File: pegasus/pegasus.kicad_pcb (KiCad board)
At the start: 2 copper layers, 50 x 120 mm, 10 parts, among them IC1 RFD900, IC2 Adafruit_MPL3115A2, IC3 Adafruit-BNO055-PCB, IC4 L70B-M39, IC5 L7805ACV, J1 Conn_01x02_Female, J2 Conn_01x02_Female, U1 Teensy4.1, U2 CON-SMA-EDGE-S, U3 CON-SMA-EDGE-S

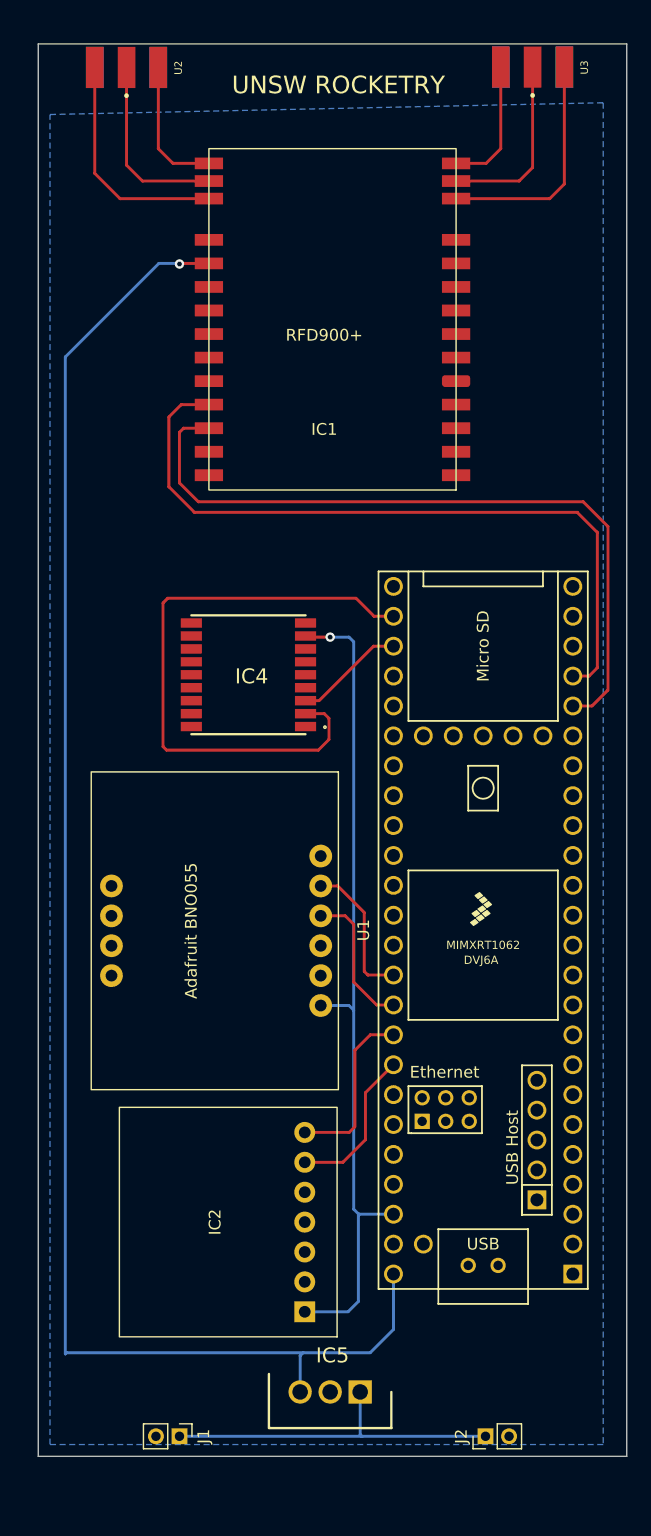
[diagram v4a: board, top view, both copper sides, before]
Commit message: added ground plane and vias. completed trace routing
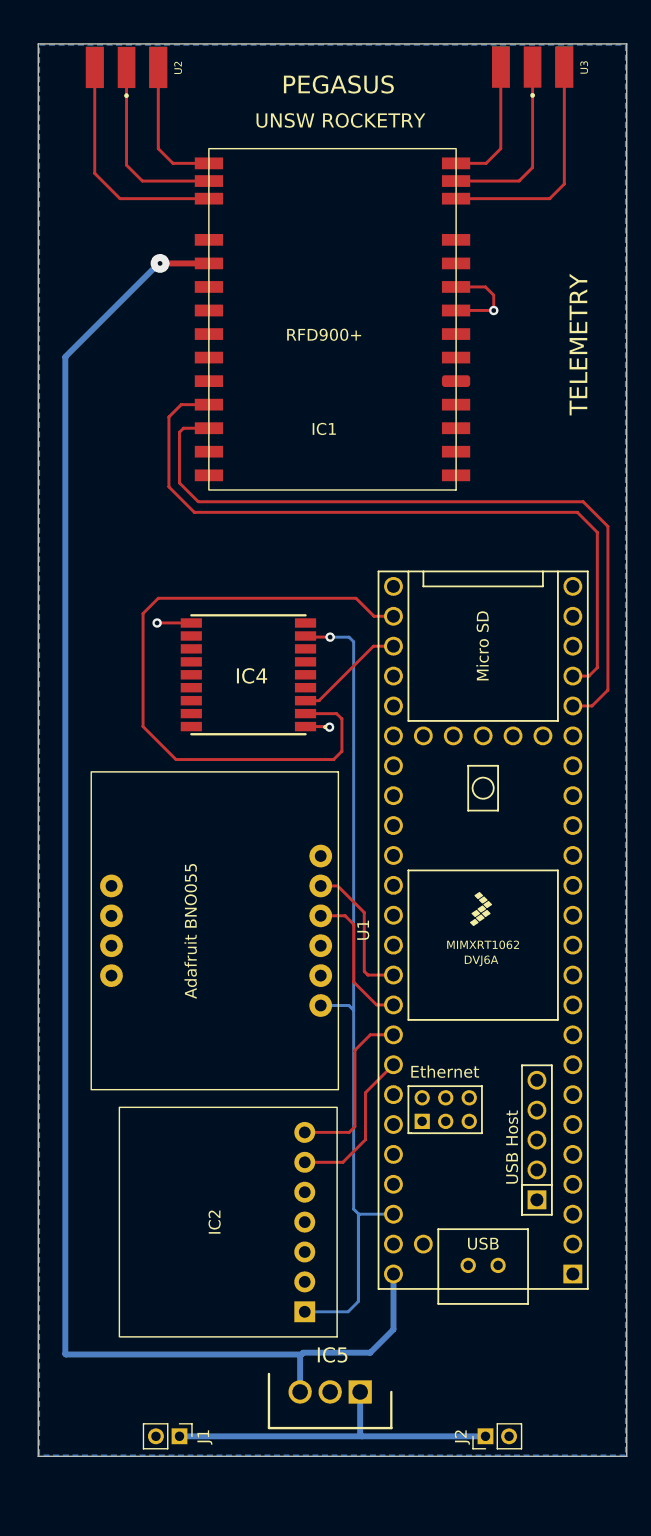
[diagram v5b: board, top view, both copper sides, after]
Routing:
- net GND: track 0.00 -> 13.0 mm, vias 0 -> 3
- net RX8: track 51.1 -> 56.4 mm
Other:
- board text added: "PEGASUS"
- board text added: "TELEMETRY"
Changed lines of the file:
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@@
   )
   (gr_rect (start 130 160) (end 80 40) (layer "Edge.Cuts") (width 0.1) (fill none))
-  (gr_text "UNSW ROCKETRY" (at 105.5 43.5) (layer "F.SilkS")
+  (gr_text "TELEMETRY\n" (at 125.95 65.55 90) (layer "F.SilkS")
     (effects (font (size 1.5 1.5) (thickness 0.3)))
   )
+  (gr_text "PEGASUS\n" (at 105.5 43.5) (layer "F.SilkS")
+    (effects (font (size 1.5 1.5) (thickness 0.3)))
+  )
+  (gr_text "UNSW ROCKETRY\n" (at 105.65 46.55) (layer "F.SilkS")
+    (effects (font (size 1.2 1.2) (thickness 0.2)))
+  )
+  (segment (start 118.7 61.35) (end 118.7 62.65) (width 0.25) (layer "F.Cu") (net 2))
+  (segment (start 115.5 60.65) (end 118 60.65) (width 0.25) (layer "F.Cu") (net 2))
+  (segment (start 104.7 98) (end 104.75 98.05) (width 0.25) (layer "F.Cu") (net 2))
+  (segment (start 118 60.65) (end 118.7 61.35) (width 0.25) (layer "F.Cu") (net 2))
+  (segment (start 90.1 89.2) (end 93.007 89.2) (width 0.25) (layer "F.Cu") (net 2))
+  (segment (start 102.707 98) (end 104.7 98) (width 0.25) (layer "F.Cu") (net 2))
+  (segment (start 115.5 62.65) (end 118.7 62.65) (width 0.25) (layer "F.Cu") (net 2))
+  (via (at 104.75 98.05) (size 0.8) (drill 0.4) (layers "F.Cu" "B.Cu") (free) (net 2))
+  (via (at 118.7 62.65) (size 0.8) (drill 0.4) (layers "F.Cu" "B.Cu") (net 2))
+  (via (at 90.1 89.2) (size 0.8) (drill 0.4) (layers "F.Cu" "B.Cu") (free) (net 2))
   (segment (start 124.7 51.9) (end 124.7 41.9725) (width 0.25) (layer "F.Cu") (net 11))
   (segment (start 123.45 53.15) (end 124.7 51.9) (width 0.25) (layer "F.Cu") (net 11))
@@
   (segment (start 84.8 51) (end 84.8 42) (width 0.25) (layer "F.Cu") (net 16))
   (segment (start 107.5 158.3) (end 107.35 158.15) (width 0.25) (layer "B.Cu") (net 90))
-  (segment (start 118 158.3) (end 107.5 158.3) (width 0.25) (layer "B.Cu") (net 90))
-  (segment (start 107.35 158.15) (end 107.35 154.53) (width 0.25) (layer "B.Cu") (net 90))
-  (segment (start 107.5 158.3) (end 92 158.3) (width 0.25) (layer "B.Cu") (net 90))
-  (segment (start 91 87.1) (end 107 87.1) (width 0.25) (layer "F.Cu") (net 99))
-  (segment (start 90.6 87.5) (end 91 87.1) (width 0.25) (layer "F.Cu") (net 99))
-  (segment (start 104.7 99.1) (end 103.8 100) (width 0.25) (layer "F.Cu") (net 99))
-  (segment (start 102.707 96.9) (end 104.3 96.9) (width 0.25) (layer "F.Cu") (net 99))
+  (segment (start 118 158.3) (end 107.5 158.3) (width 0.5) (layer "B.Cu") (net 90))
+  (segment (start 107.35 158.15) (end 107.35 154.53) (width 0.5) (layer "B.Cu") (net 90))
+  (segment (start 107.5 158.3) (end 92 158.3) (width 0.5) (layer "B.Cu") (net 90))
+  (segment (start 91.7 100.8) (end 88.9 98) (width 0.25) (layer "F.Cu") (net 99))
+  (segment (start 105.8 97.35) (end 105.8 100.1) (width 0.25) (layer "F.Cu") (net 99))
+  (segment (start 88.9 88.4) (end 90.2 87.1) (width 0.25) (layer "F.Cu") (net 99))
   (segment (start 107 87.1) (end 108.53 88.63) (width 0.25) (layer "F.Cu") (net 99))
-  (segment (start 90.6 99.7) (end 90.6 87.5) (width 0.25) (layer "F.Cu") (net 99))
-  (segment (start 103.8 100) (end 90.9 100) (width 0.25) (layer "F.Cu") (net 99))
   (segment (start 108.53 88.63) (end 110.18 88.63) (width 0.25) (layer "F.Cu") (net 99))
-  (segment (start 90.9 100) (end 90.6 99.7) (width 0.25) (layer "F.Cu") (net 99))
-  (segment (start 104.7 97.3) (end 104.7 99.1) (width 0.25) (layer "F.Cu") (net 99))
-  (segment (start 104.3 96.9) (end 104.7 97.3) (width 0.25) (layer "F.Cu") (net 99))
+  (segment (start 88.9 98) (end 88.9 88.4) (width 0.25) (layer "F.Cu") (net 99))
+  (segment (start 105.35 96.9) (end 105.8 97.35) (width 0.25) (layer "F.Cu") (net 99))
+  (segment (start 105.1 100.8) (end 91.7 100.8) (width 0.25) (layer "F.Cu") (net 99))
+  (segment (start 90.2 87.1) (end 107 87.1) (width 0.25) (layer "F.Cu") (net 99))
+  (segment (start 102.707 96.9) (end 105.35 96.9) (width 0.25) (layer "F.Cu") (net 99))
+  (segment (start 105.8 100.1) (end 105.1 100.8) (width 0.25) (layer "F.Cu") (net 99))
   (segment (start 103.857 95.8) (end 108.487 91.17) (width 0.25) (layer "F.Cu") (net 100))
   (segment (start 102.707 95.8) (end 103.857 95.8) (width 0.25) (layer "F.Cu") (net 100))
@@
   (segment (start 107.7 113.8) (end 107.7 118.8) (width 0.25) (layer "F.Cu") (net 107))
   (segment (start 104 111.54) (end 105.44 111.54) (width 0.25) (layer "F.Cu") (net 107))
-  (segment (start 92 58.6) (end 92.05 58.65) (width 0.25) (layer "F.Cu") (net 108))
-  (segment (start 92.05 58.65) (end 94.5 58.65) (width 0.25) (layer "F.Cu") (net 108))
-  (via (at 92 58.7) (size 0.8) (drill 0.4) (layers "F.Cu" "B.Cu") (net 108))
-  (segment (start 102.5 151.2) (end 82.4 151.2) (width 0.25) (layer "B.Cu") (net 108))
-  (segment (start 110.18 149.22) (end 110.18 144.51) (width 0.25) (layer "B.Cu") (net 108))
-  (segment (start 91.95 58.65) (end 92 58.7) (width 0.25) (layer "B.Cu") (net 108))
+  (segment (start 90.35 58.65) (end 94.5 58.65) (width 0.5) (layer "F.Cu") (net 108))
+  (via (at 90.35 58.65) (size 1.6) (drill 0.4) (layers "F.Cu" "B.Cu") (net 108))
+  (segment (start 102.35 151.35) (end 82.35 151.35) (width 0.5) (layer "B.Cu") (net 108))
+  (segment (start 110.18 149.22) (end 110.18 144.51) (width 0.5) (layer "B.Cu") (net 108))
+  (segment (start 82.35 151.35) (end 82.3 151.3) (width 0.5) (layer "B.Cu") (net 108))
   (segment (start 102.25 151.45) (end 102.5 151.2) (width 0.25) (layer "B.Cu") (net 108))
-  (segment (start 82.3 151.3) (end 82.3 66.6) (width 0.25) (layer "B.Cu") (net 108))
-  (segment (start 90.25 58.65) (end 91.95 58.65) (width 0.25) (layer "B.Cu") (net 108))
-  (segment (start 102.25 154.53) (end 102.25 151.45) (width 0.25) (layer "B.Cu") (net 108))
-  (segment (start 108.2 151.2) (end 110.18 149.22) (width 0.25) (layer "B.Cu") (net 108))
+  (segment (start 82.3 151.3) (end 82.3 66.6) (width 0.5) (layer "B.Cu") (net 108))
+  (segment (start 102.25 154.53) (end 102.25 151.45) (width 0.5) (layer "B.Cu") (net 108))
+  (segment (start 102.5 151.2) (end 102.35 151.35) (width 0.5) (layer "B.Cu") (net 108))
+  (segment (start 108.2 151.2) (end 110.18 149.22) (width 0.5) (layer "B.Cu") (net 108))
   (segment (start 82.4 151.2) (end 82.3 151.3) (width 0.25) (layer "B.Cu") (net 108))
-  (segment (start 102.5 151.2) (end 108.2 151.2) (width 0.25) (layer "B.Cu") (net 108))
-  (segment (start 82.3 66.6) (end 90.25 58.65) (width 0.25) (layer "B.Cu") (net 108))
+  (segment (start 102.5 151.2) (end 108.2 151.2) (width 0.5) (layer "B.Cu") (net 108))
+  (segment (start 82.3 66.6) (end 90.25 58.65) (width 0.5) (layer "B.Cu") (net 108))
   (zone (net 2) (net_name "GND") (layer "B.Cu") (hatch edge 0.508)
+    (priority 1)
     (connect_pads (clearance 0.508))
-    (min_thickness 0.254)
-    (fill (thermal_gap 0.508) (thermal_bridge_width 0.508))
+    (min_thickness 0.254) (filled_areas_thickness no)
+    (fill yes (thermal_gap 0.508) (thermal_bridge_width 0.508))
     (polygon
       (pts
-        (xy 128 159)
-        (xy 81 159)
-        (xy 81 46)
-        (xy 128 45)
+        (xy 129.9 159.9)
+        (xy 80.1 159.9)
+        (xy 80.1 40.1)
+        (xy 129.9 40.1)
       )
     )

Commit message: adjusted trace width for 5V power, added mounting holes, some 3D models
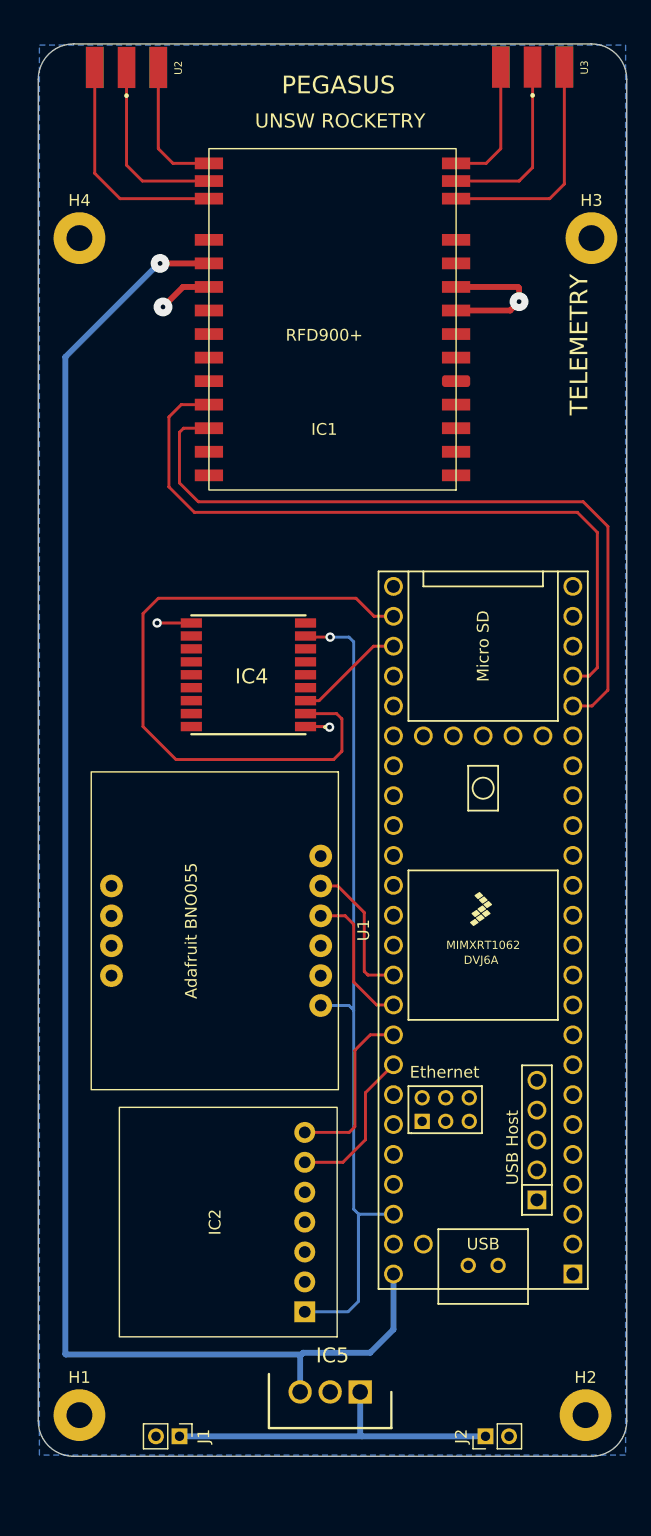
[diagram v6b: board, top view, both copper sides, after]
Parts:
- added H1: MountingHole_Pad, MountingHole:MountingHole_2.2mm_M2_Pad, F.Cu at (83.5, 156.5)
- added H2: MountingHole_Pad, MountingHole:MountingHole_2.2mm_M2_Pad, F.Cu at (126.5, 156.5)
- added H3: MountingHole_Pad, MountingHole:MountingHole_2.2mm_M2_Pad, F.Cu at (127.0, 56.5)
- added H4: MountingHole_Pad, MountingHole:MountingHole_2.2mm_M2_Pad, F.Cu at (83.5, 56.5)
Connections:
- IC1 pad 11: unconnected-(IC1-Pad11) -> GND
- IC1 pad 20: unconnected-(IC1-Pad20) -> GND
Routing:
- net GND: track 13.0 -> 21.8 mm, vias 3 -> 4
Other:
- outline, holes or cut-outs redrawn

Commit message: added logo and cleaned up some  silkscreens on PCB
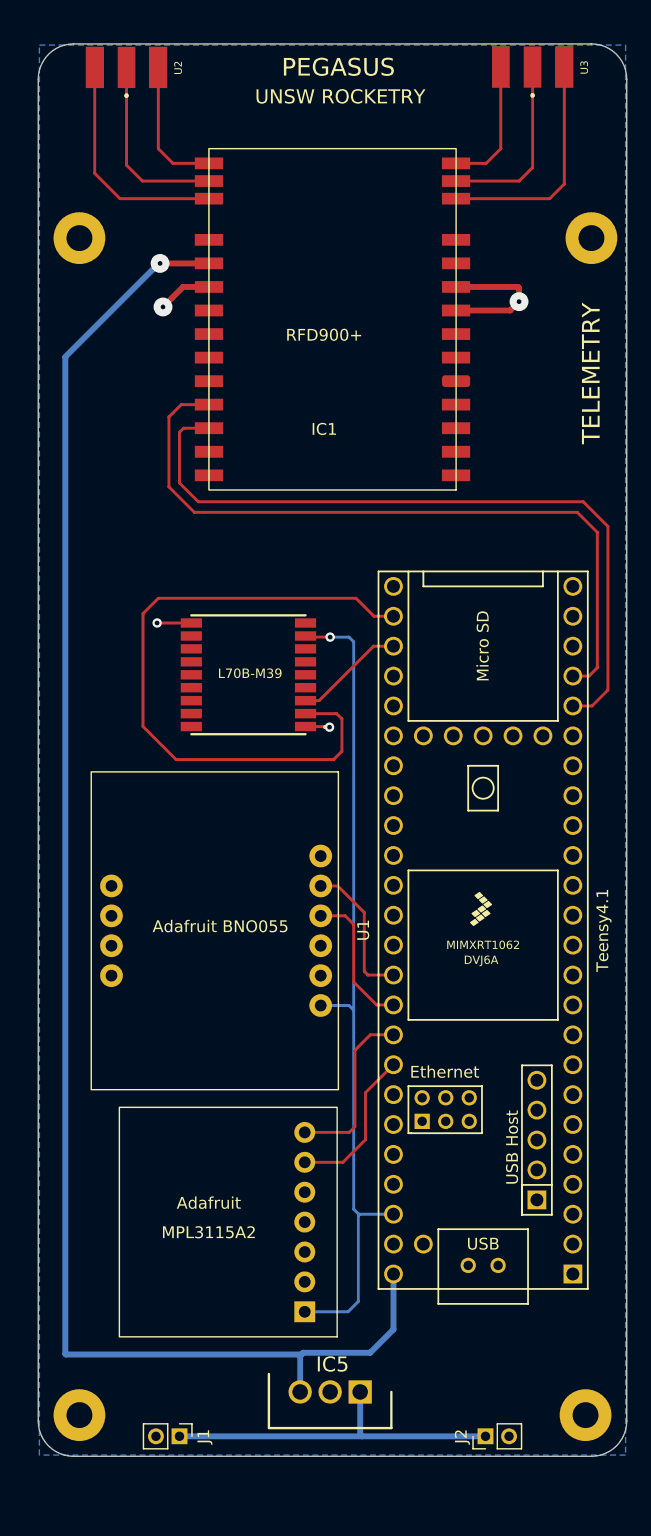
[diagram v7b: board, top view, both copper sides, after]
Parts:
- added G***: LOGO, logo:logo, B.Cu at (105.0, 58.5)
- IC2: value Adafruit_MPL3115A2 -> Adafruit
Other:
- board text added: "MPL3115A2"
